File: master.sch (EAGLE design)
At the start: 74 parts, among them M1 DHT22-NP, M2 NRF24L01P-M, Q1 IRLML2502, U1 XMEGA-A3TQFP, U2 DS1302SOIC, U3 25LC640A-E/SN, U4 ENC28J60SO, U5 TS1117, X1 serial, X2 SPI/1W, X3 I2C, X4 ADC, X6 PS25_3W-R, X7 PS25_3W-R, X8 PS25_3W-R, X9 PS25_3W-R, Y1 25MHz

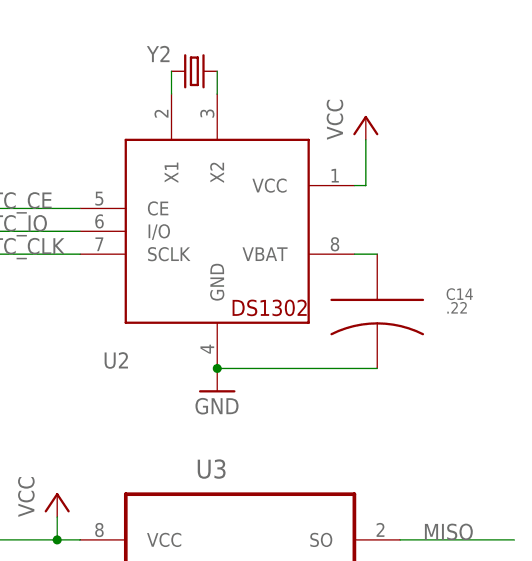
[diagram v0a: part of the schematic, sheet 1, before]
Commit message: decoupling cap for rtc
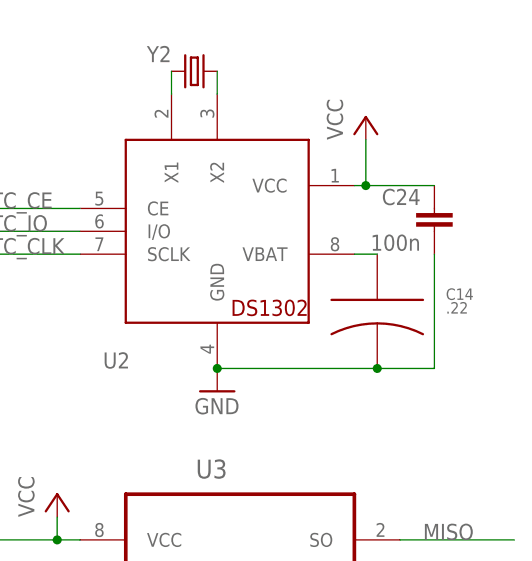
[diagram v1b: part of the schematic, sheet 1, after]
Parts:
- added C24: 100n, rcl:C-EUC0603
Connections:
- net GND: now also C24.2
- net VCC: now also C24.1
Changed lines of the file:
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@@
 <part name="GND26" library="supply1" deviceset="GND" device=""/>
 <part name="GND27" library="supply1" deviceset="GND" device=""/>
+<part name="C24" library="rcl" deviceset="C-EU" device="C0603" value="100n"/>
 </parts>
 <sheets>
@@
 <instance part="GND26" gate="1" x="128.27" y="140.97"/>
 <instance part="GND27" gate="1" x="147.32" y="140.97"/>
+<instance part="C24" gate="G$1" x="247.65" y="152.4" rot="MR0"/>
 </instances>
 <busses>
@@
 <junction x="223.52" y="134.62"/>
 <pinref part="C14" gate="G$1" pin="P$2"/>
+<pinref part="C24" gate="G$1" pin="2"/>
+<wire x1="241.3" y1="134.62" x2="247.65" y2="134.62" width="0.1524" layer="91"/>
+<wire x1="247.65" y1="134.62" x2="247.65" y2="147.32" width="0.1524" layer="91"/>
+<junction x="241.3" y="134.62"/>
 </segment>
 <segment>
@@
 <wire x1="240.03" y1="154.94" x2="240.03" y2="160.02" width="0.1524" layer="91"/>
 <pinref part="P+10" gate="VCC" pin="VCC"/>
-</segment>
-<segment>
+<pinref part="C24" gate="G$1" pin="1"/>
+<wire x1="247.65" y1="154.94" x2="240.03" y2="154.94" width="0.1524" layer="91"/>
+<junction x="240.03" y="154.94"/>
+</segment>
+<segment>

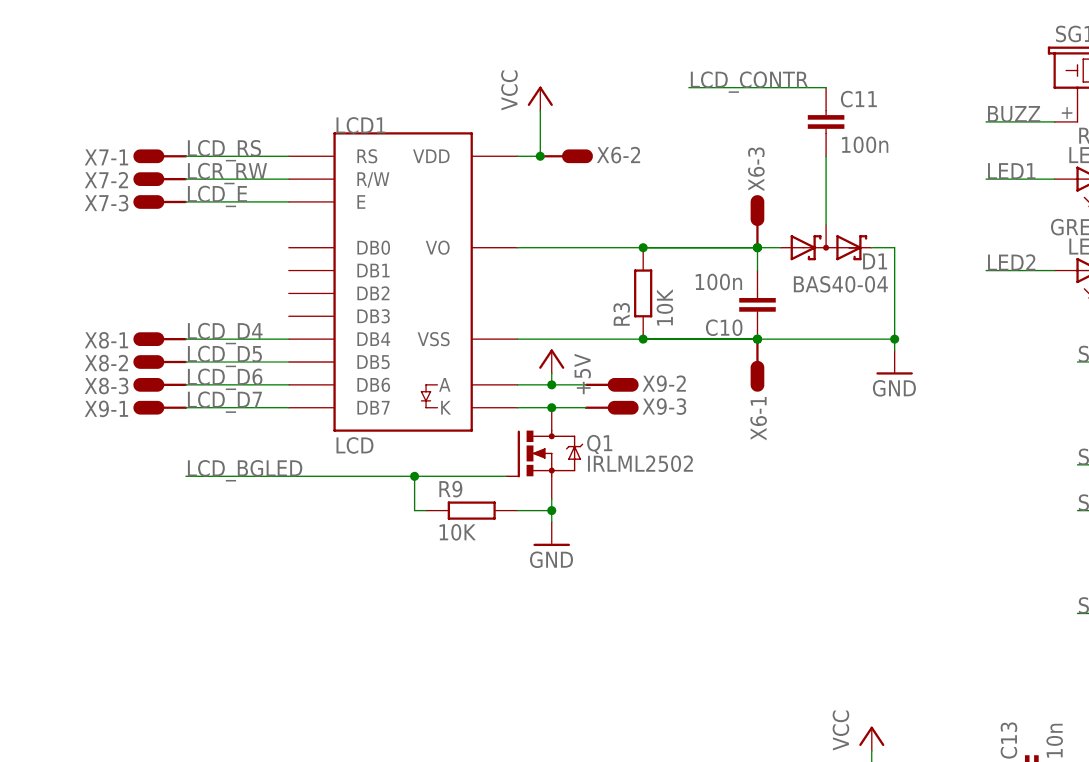
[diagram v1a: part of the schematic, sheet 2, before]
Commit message: lcd connector changed to standard 2.54 pin header
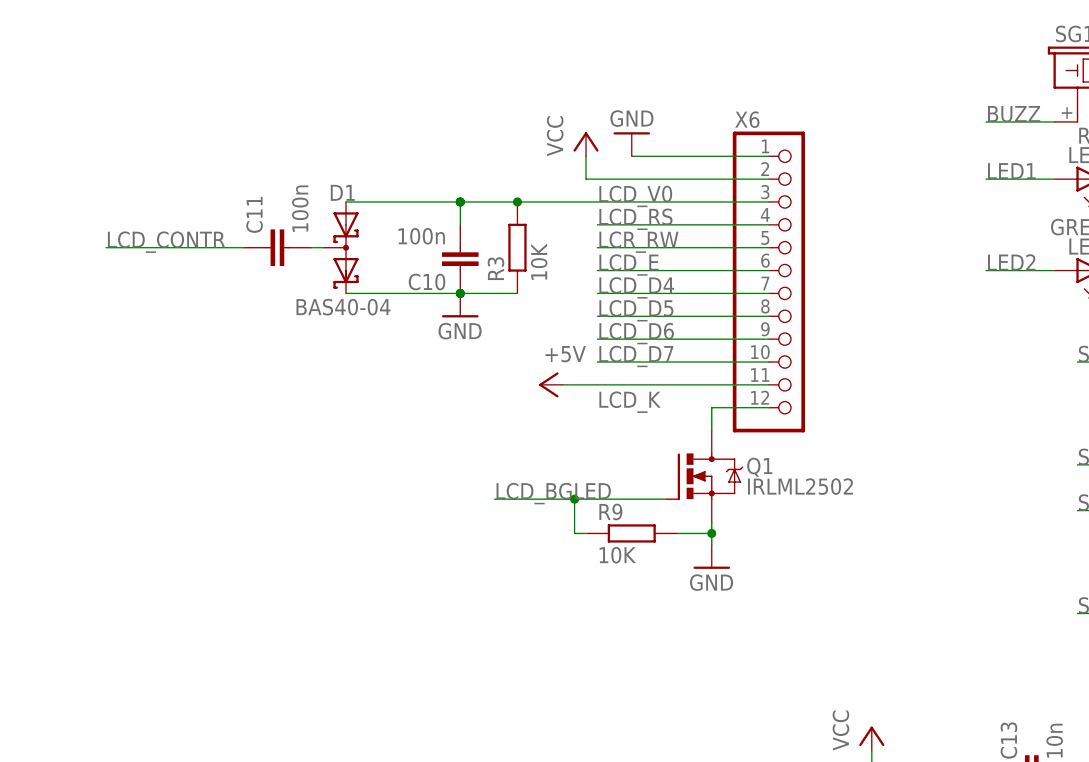
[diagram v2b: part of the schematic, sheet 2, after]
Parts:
- removed LCD1: LCD, external:LCD
- removed X7, X8, X9: PS25_3W-R, con_PS25:PS25_3W-R
- X6: value PS25_3W-R -> (none); device con_PS25:PS25_3W-R -> pinhead-mod:PINHD-1X12_2.54-R
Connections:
- removed net N$8: LCD1.K, Q1.D, X9-3.P$1
- removed net N$9: C10.2, D1.A1, LCD1.VO, R3.2, X6-3.P$1
- new net LCD_K: Q1.D, X6.12
- new net LCD_V0: C10.2, D1.A1, R3.2, X6.3
- net +5V: now also X6.11; no longer LCD1.A, X9-2.P$1
- net GND: now also X6.1; no longer LCD1.VSS, X6-1.P$1
- net LCD_D4: now also X6.7; no longer LCD1.DB4, X8-1.P$1
- net LCD_D5: now also X6.8; no longer LCD1.DB5, X8-2.P$1
- net LCD_D6: now also X6.9; no longer LCD1.DB6, X8-3.P$1
- net LCD_D7: now also X6.10; no longer LCD1.DB7, X9-1.P$1
- net LCD_E: now also X6.6; no longer LCD1.E, X7-3.P$1
- net LCD_RS: now also X6.4; no longer LCD1.RS, X7-1.P$1
- net LCR_RW: now also X6.5; no longer LCD1.R/W, X7-2.P$1
- net VCC: now also X6.2; no longer LCD1.VDD, X6-2.P$1
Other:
- moved on the sheet: C10, C11, D1, Q1, R3, R9

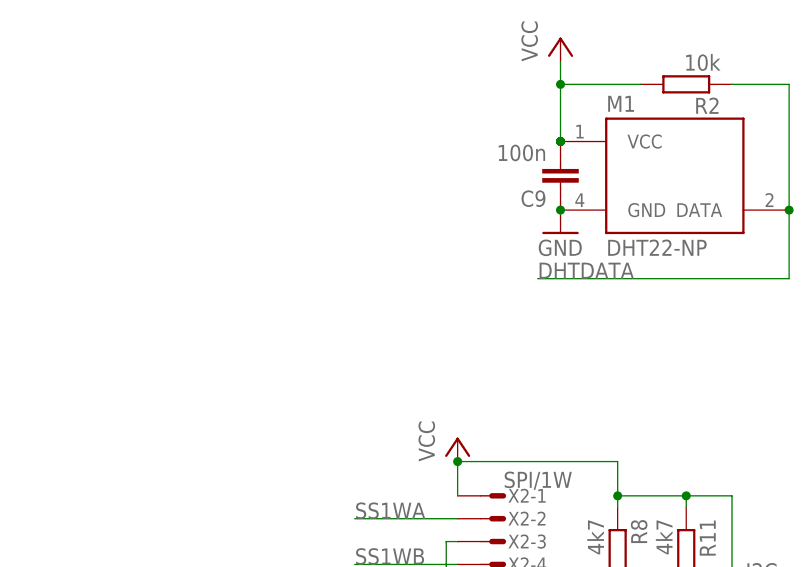
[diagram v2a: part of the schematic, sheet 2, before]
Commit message: dht22 sometimes hang, add mosfet as low side reset switch
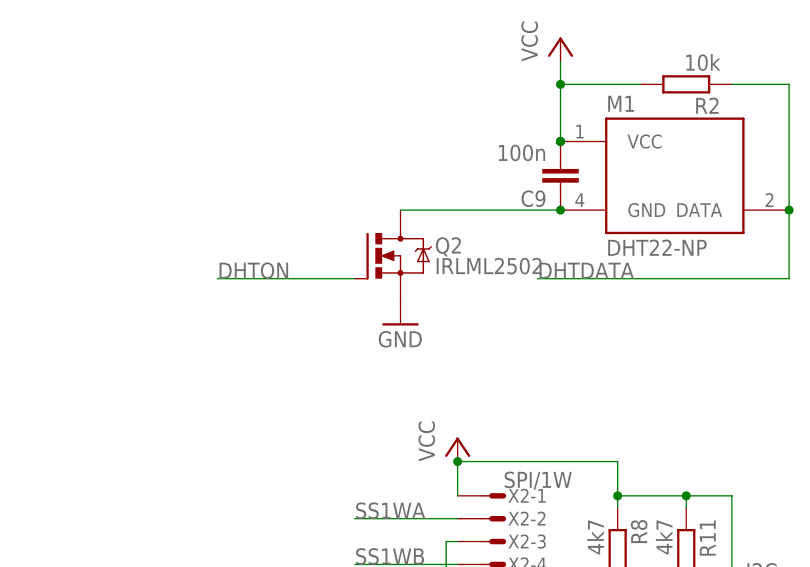
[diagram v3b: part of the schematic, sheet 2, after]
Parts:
- added Q2: IRLML2502, mosfet:IRLML2502
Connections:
- new net DHTON: Q2.G, U1.PC0(OC0A/SDA)
- new net N$8: C9.1, M1.GND, Q2.D
- net !LANCS: now also U1.PD0(OC0A); no longer U1.PC7(SCK/TXD1/CLKO/EVO)
- net !LANINT: now also U1.PC7(SCK/TXD1/CLKO/EVO); no longer U1.PC6(MISO/RXD1)
- net !RFCS: now also U1.PD2(OC0C/RXD0); no longer U1.PD1(OC0B/XCK0)
- net GND: now also Q2.S; no longer C9.1, M1.GND
- net LCD_BGLED: now also U1.PC2(OC0C/RXD0); no longer U1.PC1(OC0B/XCK0/SCL)
- net LCD_CONTR: now also U1.PC1(OC0B/XCK0/SCL); no longer U1.PC0(OC0A/SDA)
- net RFCE: now also U1.PD3(OC0D/TXD0); no longer U1.PD2(OC0C/RXD0)
- net RFIRQ: now also U1.PD1(OC0B/XCK0); no longer U1.PD0(OC0A)
- net S1A: now also U1.PC6(MISO/RXD1); no longer U1.PC5(OC1B/MOSI/XCK1)
- net S1B: now also U1.PC5(OC1B/MOSI/XCK1); no longer U1.PC4(OC1A/!SS!)
- net S1P: now also U1.PC4(OC1A/!SS!); no longer U1.PC3(OC0D/TXD0)
- net S2: now also U1.PC3(OC0D/TXD0); no longer U1.PC2(OC0C/RXD0)
